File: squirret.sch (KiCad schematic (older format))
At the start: 13 parts

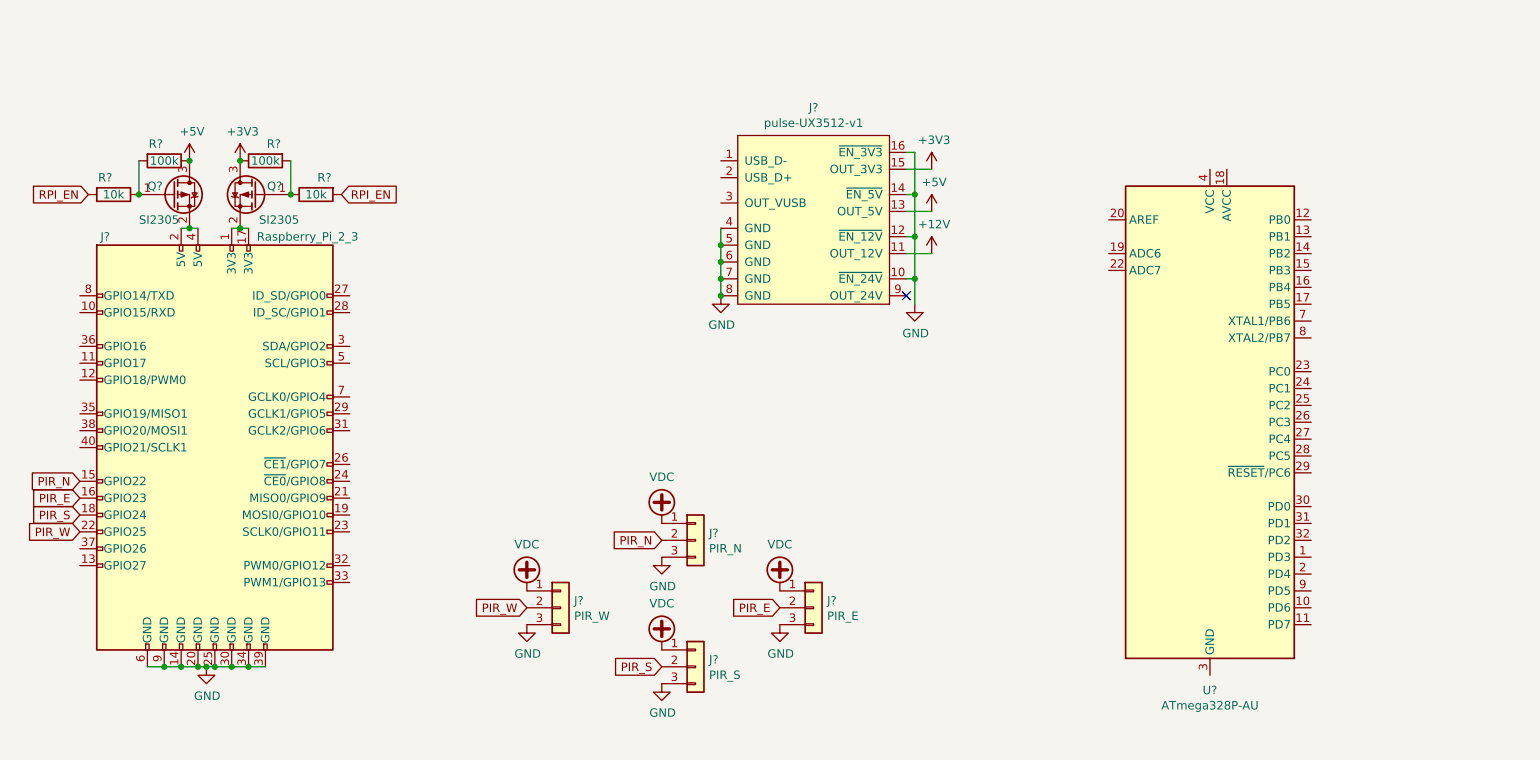
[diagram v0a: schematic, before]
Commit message: Add 328P
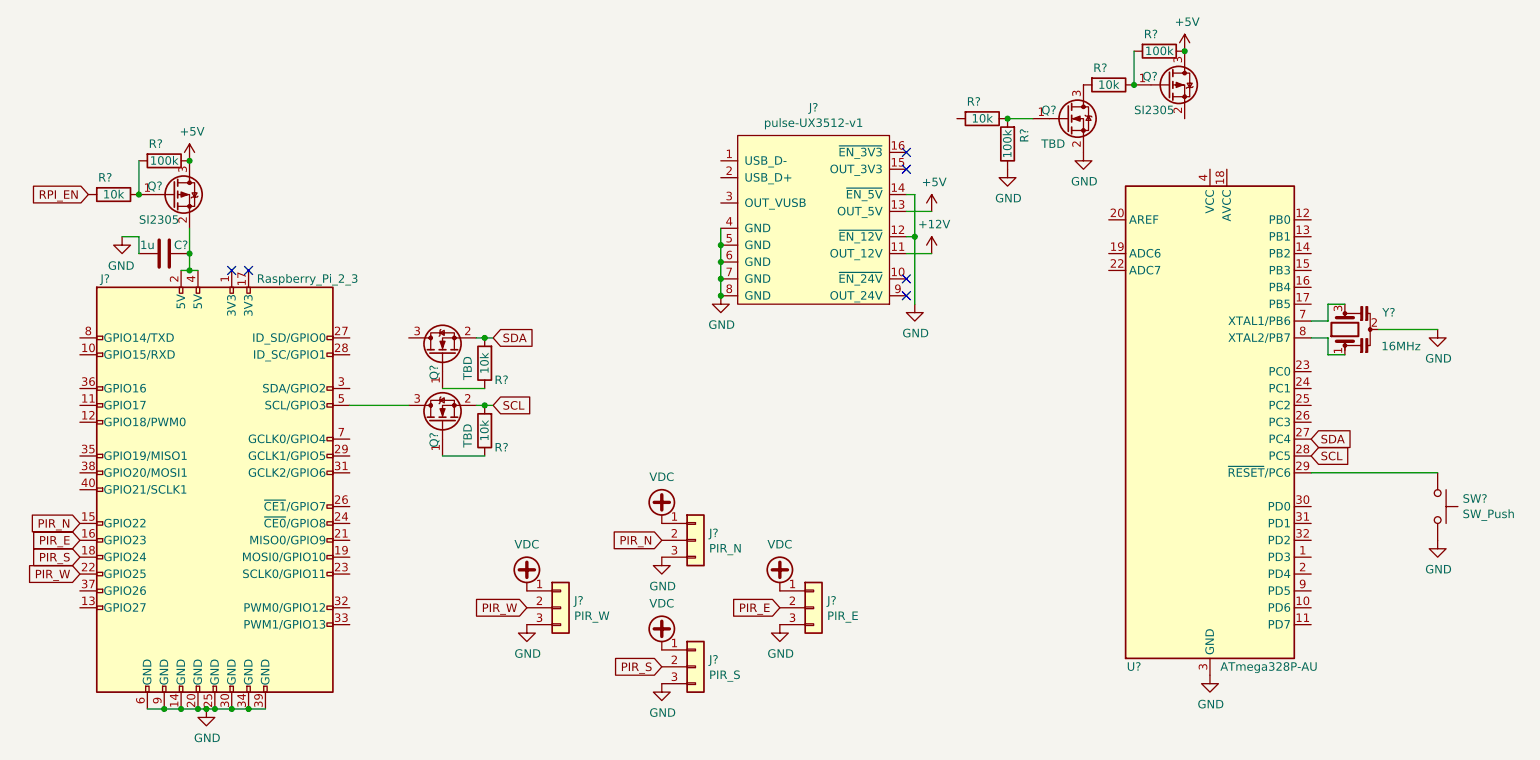
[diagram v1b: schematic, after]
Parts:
- removed Q?: SI2305, symbol Device:Q_PMOS_GSD
- removed R?: 100k, symbol Device:R
- removed R?: 10k, symbol Device:R
- added C?: 1u, symbol Device:C
- added Q?: SI2305, symbol Device:Q_PMOS_GSD
- added Q? (x3): TBD, symbol Device:Q_NMOS_GSD
- added R? (x2): 100k, symbol Device:R
- added R? (x4): 10k, symbol Device:R
- added SW?: SW_Push, symbol Switch:SW_Push
- added Y?: 16MHz, symbol Device:Resonator
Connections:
- net +5V: now also Q?.3 (D), R?.1
- net GND: now also U?.21 (GND), U?.3 (GND), U?.5 (GND), C?.1, Q?.2 (S), R?.1, SW?.2, Y?.2; no longer J?.10 (~EN_24V), J?.16 (~EN_3V3)
- net at J?.1 (3V3): no longer J?.17 (3V3)
- net at J?.2 (5V), J?.4 (5V), Q?.2 (S): now also C?.2
- net at J?.5 (SCL/GPIO3): now also Q?.3 (D)
- net SDA: now reaches U?.27 (PC4)
- net SDA: now also Q?.2 (S), R?.2
- net SCL: now reaches U?.28 (PC5)
- net SCL: now also Q?.2 (S), R?.2
- net at U?.29 (~RESET~/PC6): now also SW?.1
- net at U?.7 (XTAL1/PB6): now also Y?.3
- net at U?.8 (XTAL2/PB7): now also Y?.1
- net +3V3: no longer names the net of J?.15 (OUT_3V3)
- new net: Q?.1 (G), R?.1, R?.2 (x2)
- new net: Q?.3 (D), R?.2
- new net: Q?.1 (G), R?.1 (x2)
- no-connect marks 1 -> 6
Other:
- moved on the sheet: J?
